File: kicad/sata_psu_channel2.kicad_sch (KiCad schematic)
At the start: 8 parts, among them J2 12V/GND/GND/5V, Q2 AO3401A

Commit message: v2: per-port 5V buck with 0R neighbour sharing, plus rail indicators
Every port now has its own local 5V node and its own buck footprint, with
adjacent nodes joined by 0R links (R61-R64). How a port gets its 5V is a
populate choice rather than a layout one -- BUCKS/LINKS at the top of
gen_sch.py is the whole configuration, and the lands are always present.

This closes v1's largest open issue. One 3A TPS563200 was under-rated
against a five-bay 5V rail; capping a buck at a three-port group makes its
worst case 2.1A and the same part is correctly sized.

Indicators: one 12V LED on the common rail, tapped after Q8 so it also
proves the reverse-polarity guard conducts, and one 5V LED per port on the
local node at the header, so it lights whether that port's 5V came from its
own buck or across a link.

verify.py gains check 5, the rail populate rules. A DNP part is still a
wire in the netlist, so a build that fits R63 with both U2 and U4 populated
passes ERC and netlist equivalence and parallels two regulators on the
bench. Nothing else can catch it. It also refuses groups over three ports
and any link carrying more than one port's current.

Also fixed: check_layout.py reported "0 symbols checked" and PASSED after
KiCad re-saved the sheets in its own format, because text[text.find(m):]
yields the last character rather than "" when the marker is absent, so the
`or text` fallback never fired. It now fails loudly when it parses nothing.

Schematic verified (ERC clean, 50 nets equivalent to the independent SKiDL
description, pins match pads). Board placed at 64.9 x 76.0 mm, 112 parts,
0 DRC violations. Routing still not started.

Co-Authored-By: Claude Opus 5 <noreply@anthropic.com>
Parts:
- removed D2: 8.2V, Diode_SMD:D_SOD-123, symbol Device:D_Zener
- removed R2: 220k, Resistor_SMD:R_0603_1608Metric, symbol Device:R
- added C24: 10uF/50V, Capacitor_SMD:C_1206_3216Metric, symbol Device:C
- added C25, C26: 100nF, Capacitor_SMD:C_0603_1608Metric, symbol Device:C
- added C27, C28: 22uF/25V, Capacitor_SMD:C_1206_3216Metric, symbol Device:C
- added D21: 8.2V, Diode_SMD:D_SOD-123, symbol Device:D_Zener
- added D22: GRN, LED_SMD:LED_0603_1608Metric, symbol Device:LED
- added L2: 4.7uH/4.5A, Inductor_SMD:L_Bourns_SRN6045TA, symbol Device:L
- added R21: 220k, Resistor_SMD:R_0603_1608Metric, symbol Device:R
- added R22: 56k, Resistor_SMD:R_0603_1608Metric, symbol Device:R
- added R23: 10k, Resistor_SMD:R_0603_1608Metric, symbol Device:R
- added R24: 100k, Resistor_SMD:R_0603_1608Metric, symbol Device:R
- added R25: 1.5k, Resistor_SMD:R_0603_1608Metric, symbol Device:R
- added U2: TPS563200, Package_TO_SOT_SMD:SOT-23-6, symbol Regulator_Switching:TPS563200
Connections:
- net 12V_MAIN: now also C24.1, C25.1, D21.1 (K), R24.1, U2.3 (VIN)
- net GND: now also C24.2, C25.2, C27.2, C28.2, R21.2, R23.2, R25.2, U2.1 (GND)
- net at C21.2, Q2.1 (G): now also D21.2 (A), R21.1
- net 5V_MAIN renamed 5V_2
- net 5V_2: now also C27.1, C28.1, D22.2 (A), L2.2, R22.1
- new net: R22.2, R23.1, U2.4 (VFB)
- new net: C26.1, L2.1, U2.2 (SW)
- new net: C26.2, U2.6 (VBST)
- new net: R24.2, U2.5 (EN)
- new net: D22.1 (K), R25.1
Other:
- note added: "(5 - 2.0) / 1.5k = 2.0mA"
- note added: "C21=2.2uF with R21=220k sets turn-on at ~0.5s"
- note added: "Channel 2 - staggered high-side switch + local 5V"
- note added: "D21 clamps Vgs to 8.2V; AO3401A is rated +/-12V"
- note added: "Max load is a 3-port group; see BUCKS/LINKS in gen_sch.py"
- note added: "Port 2 local 5V buck"
- note added: "Vout = 0.768V x (1 + R22/R23) = 0.768 x (1 + 56k/10k) = 5.07V"
- note removed: "C21=2.2uF with R2=220k sets turn-on at ~0.5s"
- note removed: "Channel 2 - staggered high-side switch"
- note removed: "D2 clamps Vgs to 8.2V; AO3401A is rated +/-12V"

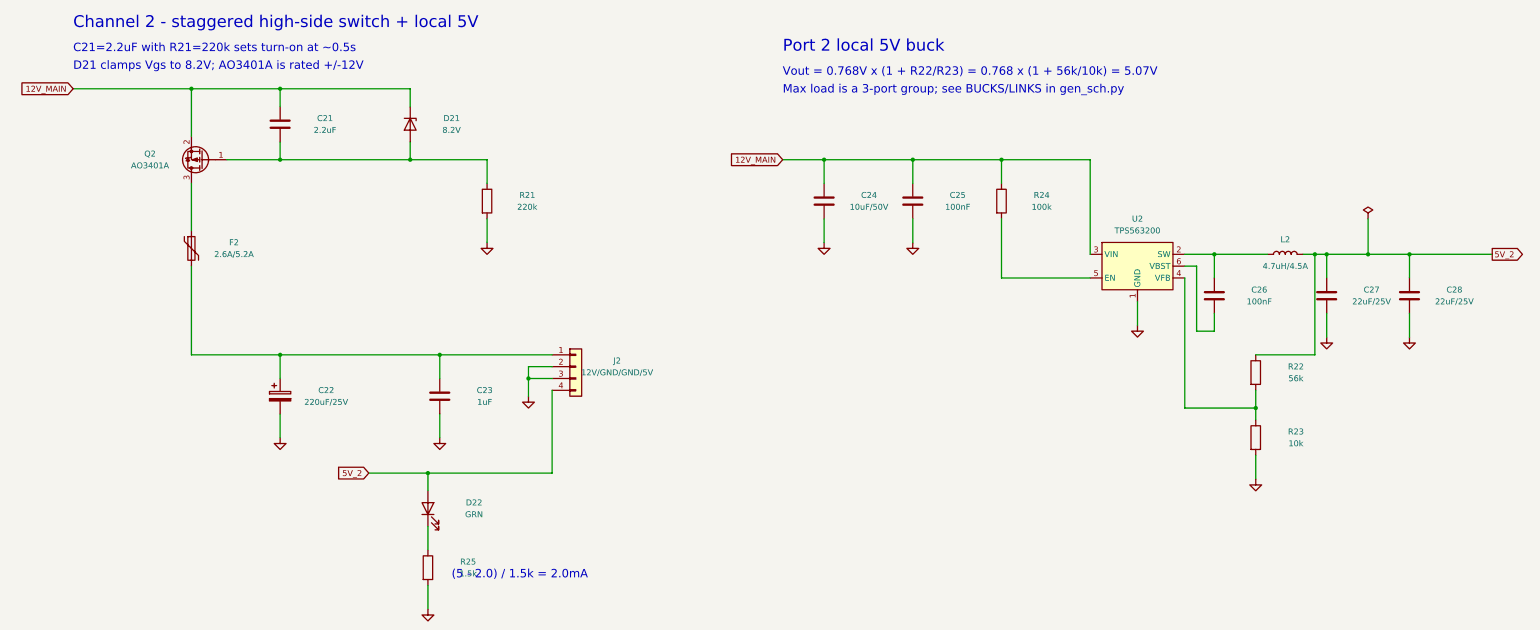
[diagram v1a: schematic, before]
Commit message: v3: JLCPCB-ready layout, fab outputs and DigiKey BOM
Board (DRC clean against JLCPCB standard 2-layer rules, 0 errors,
0 unconnected, schematic parity clean):
- design rules set to JLCPCB limits; extra pad rules in sata_psu.kicad_dru
- buck GND pins (U1-U5) were on isolated F.Cu islands: stitched to B.Cu
- C41/C51 1206 pads restored from 0603 pitch to library land pattern
- replicated SW via patches re-netted (ch2/4/5), missing ones added
- duplicate 12V zone and dangling vias on ch1 removed; 0.4 vias -> 0.45
- gate-cap courtyards in ch4/ch5 cleared; DNP flags synced from schematic
- refdes resized to 1.0/0.15 mm and placed clear of pads and silk

Outputs: Gerbers + Excellon drill (gerbers/, sata_psu_jlcpcb.zip) and
DigiKey BOM with in-stock substitutes plus a cart upload CSV.

Co-Authored-By: Claude Opus 5.5 <noreply@anthropic.com>
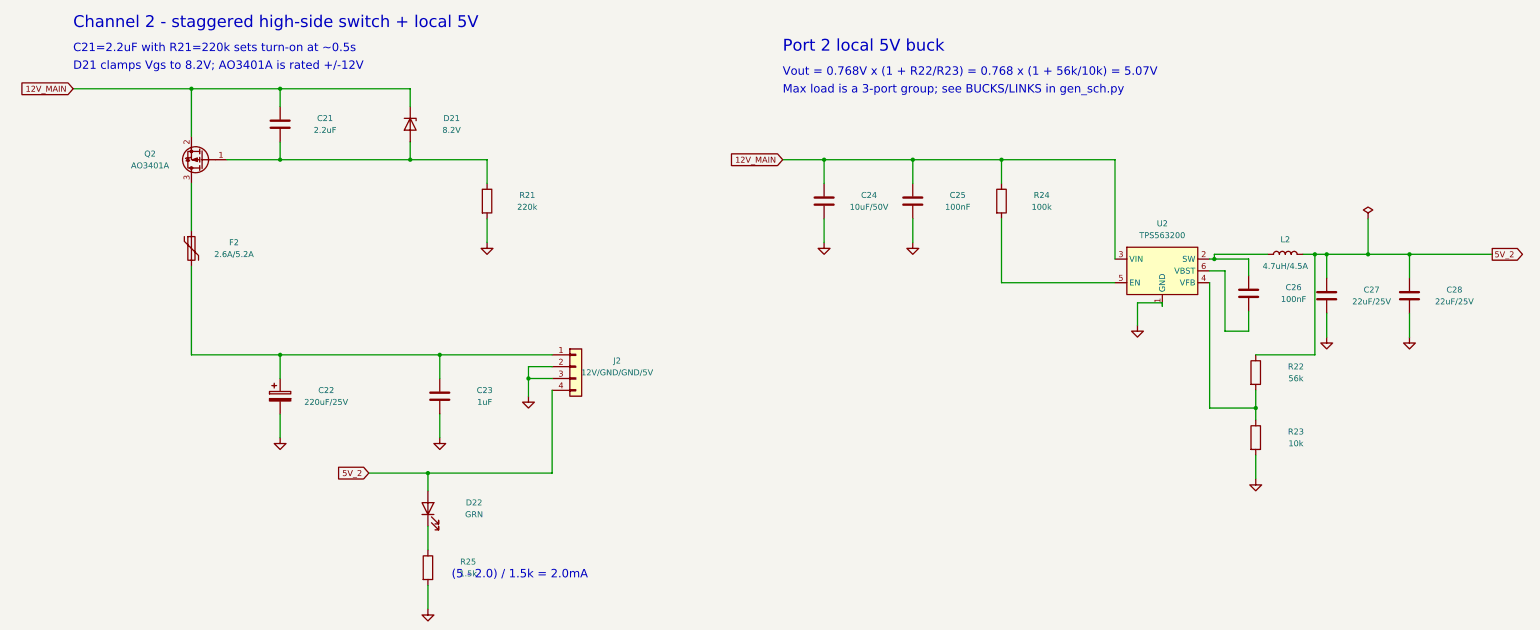
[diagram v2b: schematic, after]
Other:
- moved on the sheet: C26, U2
